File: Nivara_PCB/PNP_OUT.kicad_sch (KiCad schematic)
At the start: 0 parts

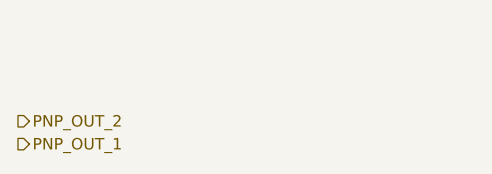
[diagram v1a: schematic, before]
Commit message: Añadido de funciones NPN/PNP
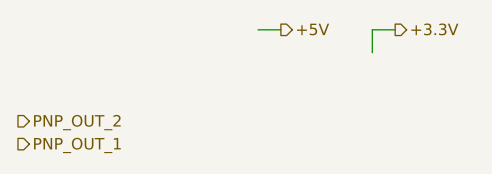
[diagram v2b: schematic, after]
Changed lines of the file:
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@@
 	(generator_version "9.0")
 	(paper "A4")
+	(wire
+		(pts
+			(xy 83.82 44.45) (xy 86.36 44.45)
+		)
+		(stroke
+			(width 0)
+			(type default)
+		)
+	)
+	(wire
+		(pts
+			(xy 96.52 44.45) (xy 96.52 46.99)
+		)
+		(stroke
+			(width 0)
+			(type default)
+		)
+	)
+	(wire
+		(pts
+			(xy 99.06 44.45) (xy 96.52 44.45)
+		)
+		(stroke
+			(width 0)
+			(type default)
+		)
+	)
+	(hierarchical_label "+5V"
+		(shape output)
+		(at 86.36 44.45 0)
+		(effects
+			(font
+				(size 1.27 1.27)
+			)
+			(justify left)
+		)
+	)
+	(hierarchical_label "+3.3V"
+		(shape output)
+		(at 99.06 44.45 0)
+		(effects
+			(font
+				(size 1.27 1.27)
+			)
+			(justify left)
+		)
+	)
 	(hierarchical_label "PNP_OUT_2"
 		(shape output)

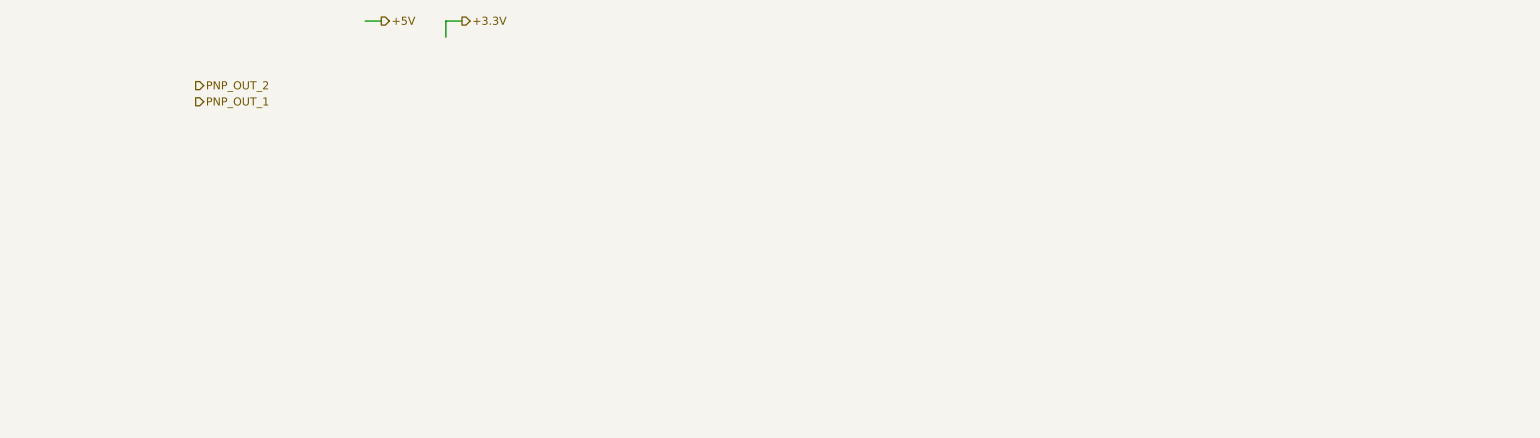
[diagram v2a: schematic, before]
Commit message: Cambios en el esquema de NPN y PNP
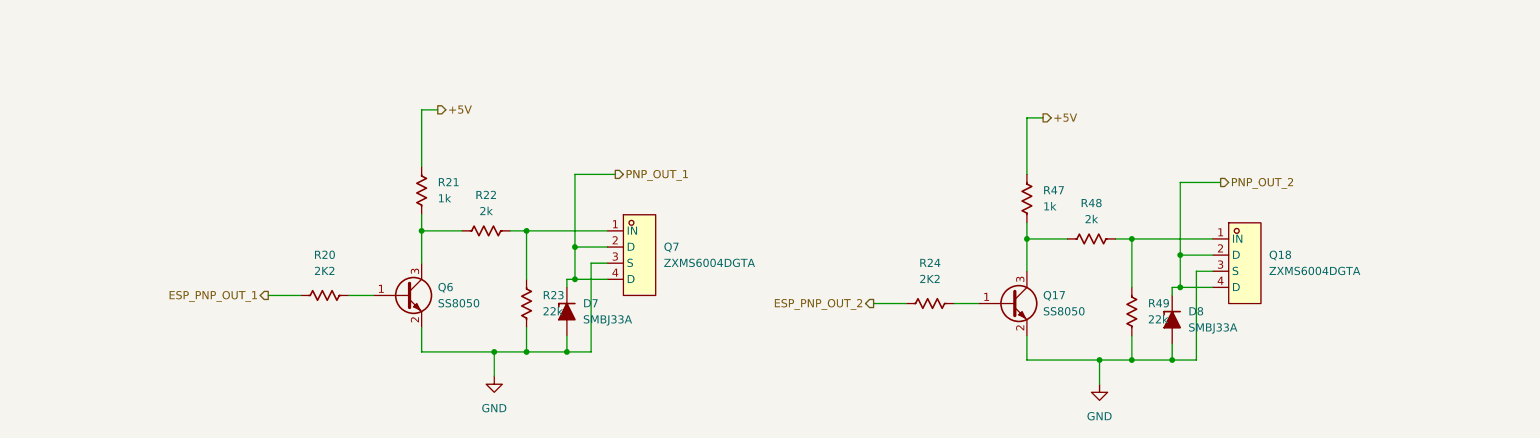
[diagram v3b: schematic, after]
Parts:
- added D7, D8: SMBJ33A, PCM_Diode_SMD_AKL:D_SMB, symbol PCM_Diode_TVS_AKL:SMBJ33A
- added Q17, Q6: SS8050, Package_TO_SOT_SMD:SOT-23, symbol Transistor_BJT:SS8050
- added Q18, Q7: ZXMS6004DGTA, Fuse_Holder:SOT-223-3_L6.5-W3.4-P2.30-LS7.0-BR, symbol Fuse_Holder:ZXMS6004DGTA
- added R20, R24: 2K2, PCM_Resistor_SMD_AKL:R_0603_1608Metric, symbol PCM_Resistor_US_AKL:R_0603
- added R21, R47: 1k, PCM_Resistor_SMD_AKL:R_0603_1608Metric, symbol PCM_Resistor_US_AKL:R_0603
- added R22, R48: 2k, PCM_Resistor_SMD_AKL:R_0603_1608Metric, symbol PCM_Resistor_US_AKL:R_0603
- added R23, R49: 22k, PCM_Resistor_SMD_AKL:R_0603_1608Metric, symbol PCM_Resistor_US_AKL:R_0603
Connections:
- net +5V: now also R21.1, R47.1
- net PNP_OUT_1: now also D7.1 (K), Q7.2 (D), Q7.4 (D)
- net PNP_OUT_2: now also D8.1 (K), Q18.2 (D), Q18.4 (D)
- new net: Q18.1 (IN), R48.2, R49.2
- new net: Q7.1 (IN), R22.2, R23.2
- new net: Q6.3 (C), R21.2, R22.1
- new net: Q17.1 (B), R24.2
- new net: Q17.3 (C), R47.2, R48.1
- new net: Q6.1 (B), R20.2
- new net ESP_PNP_OUT_1: R20.1
- new net ESP_PNP_OUT_2: R24.1
- new net GND: D7.2 (A), D8.2 (A), Q17.2 (E), Q18.3 (S), Q6.2 (E), Q7.3 (S), R23.1, R49.1

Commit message: Cambio de IntelliFet, porque los que tenían no estaban disponibles.
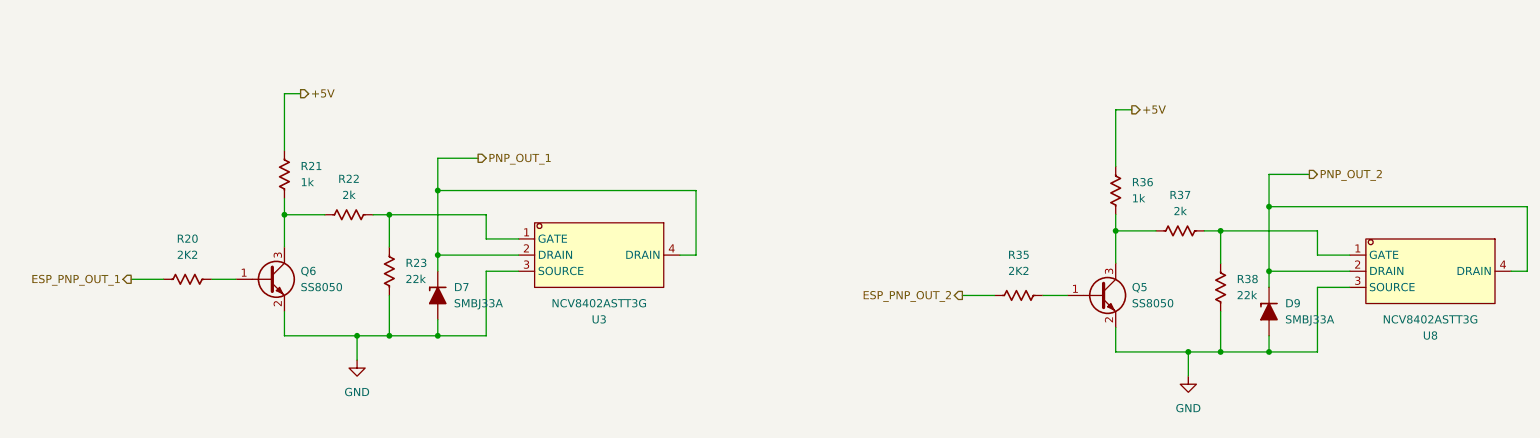
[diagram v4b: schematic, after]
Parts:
- removed D8: SMBJ33A, PCM_Diode_SMD_AKL:D_SMB, symbol PCM_Diode_TVS_AKL:SMBJ33A
- removed Q17: SS8050, Package_TO_SOT_SMD:SOT-23, symbol Transistor_BJT:SS8050
- removed Q18, Q7: ZXMS6004DGTA, Fuse_Holder:SOT-223-3_L6.5-W3.4-P2.30-LS7.0-BR, symbol Fuse_Holder:ZXMS6004DGTA
- removed R24: 2K2, PCM_Resistor_SMD_AKL:R_0603_1608Metric, symbol PCM_Resistor_US_AKL:R_0603
- removed R47: 1k, PCM_Resistor_SMD_AKL:R_0603_1608Metric, symbol PCM_Resistor_US_AKL:R_0603
- removed R48: 2k, PCM_Resistor_SMD_AKL:R_0603_1608Metric, symbol PCM_Resistor_US_AKL:R_0603
- removed R49: 22k, PCM_Resistor_SMD_AKL:R_0603_1608Metric, symbol PCM_Resistor_US_AKL:R_0603
- added D9: SMBJ33A, PCM_Diode_SMD_AKL:D_SMB, symbol PCM_Diode_TVS_AKL:SMBJ33A
- added Q5: SS8050, Package_TO_SOT_SMD:SOT-23, symbol Transistor_BJT:SS8050
- added R35: 2K2, PCM_Resistor_SMD_AKL:R_0603_1608Metric, symbol PCM_Resistor_US_AKL:R_0603
- added R36: 1k, PCM_Resistor_SMD_AKL:R_0603_1608Metric, symbol PCM_Resistor_US_AKL:R_0603
- added R37: 2k, PCM_Resistor_SMD_AKL:R_0603_1608Metric, symbol PCM_Resistor_US_AKL:R_0603
- added R38: 22k, PCM_Resistor_SMD_AKL:R_0603_1608Metric, symbol PCM_Resistor_US_AKL:R_0603
- added U3, U8: NCV8402ASTT3G, Fuse_Holder:SOT-223_L6.5-W3.5-P2.30-LS7.0-BR, symbol Fuse_Holder:NCV8402ASTT3G
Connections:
- net +5V: now also R36.1
- net ESP_PNP_OUT_2: now also R35.1
- net GND: now also D9.2 (A), Q5.2 (E), R38.1, U3.3 (SOURCE), U8.3 (SOURCE)
- net PNP_OUT_1: now also U3.2 (DRAIN), U3.4 (DRAIN)
- net PNP_OUT_2: now also D9.1 (K), U8.2 (DRAIN), U8.4 (DRAIN)
- net at R22.2, R23.2: now also U3.1 (GATE)
- new net: R37.2, R38.2, U8.1 (GATE)
- new net: Q5.3 (C), R36.2, R37.1
- new net: Q5.1 (B), R35.2
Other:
- moved on the sheet: D7, Q6, R20, R21, R22, R23

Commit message: Cambios en las salidas analogicas, ya que el ESP32 S3 no tiene DAC
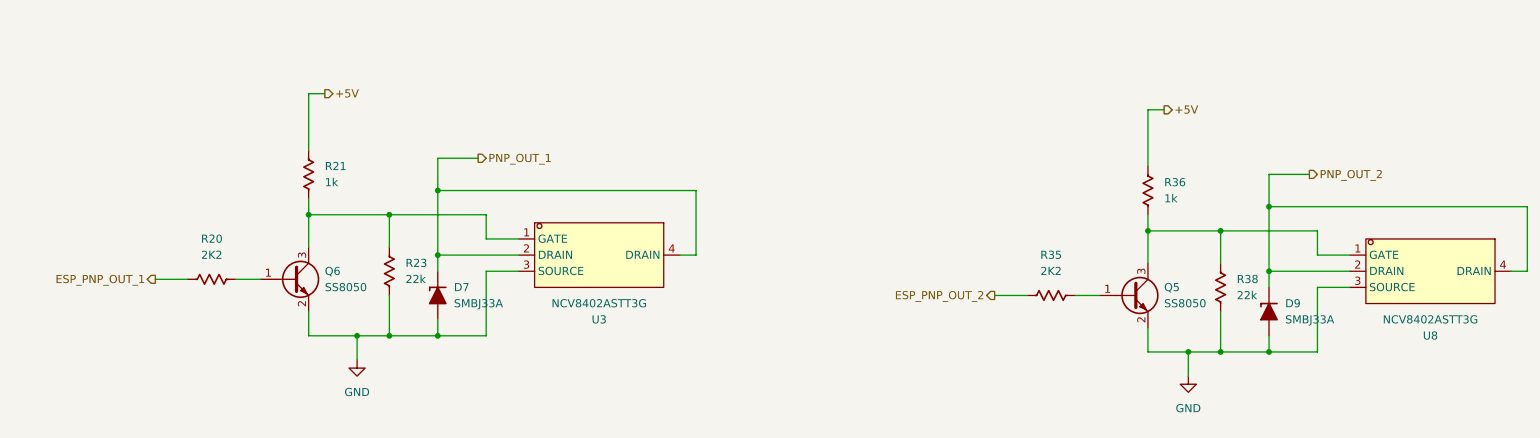
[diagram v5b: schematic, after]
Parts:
- removed R22, R37: 2k, PCM_Resistor_SMD_AKL:R_0603_1608Metric, symbol PCM_Resistor_US_AKL:R_0603
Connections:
- net at R38.2, U8.1 (GATE): now also Q5.3 (C), R36.2
- net at R23.2, U3.1 (GATE): now also Q6.3 (C), R21.2
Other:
- moved on the sheet: Q5, Q6, R20, R21, R35, R36

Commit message: Cambios en la medición de voltaje y corriente de la PCB Nivara.
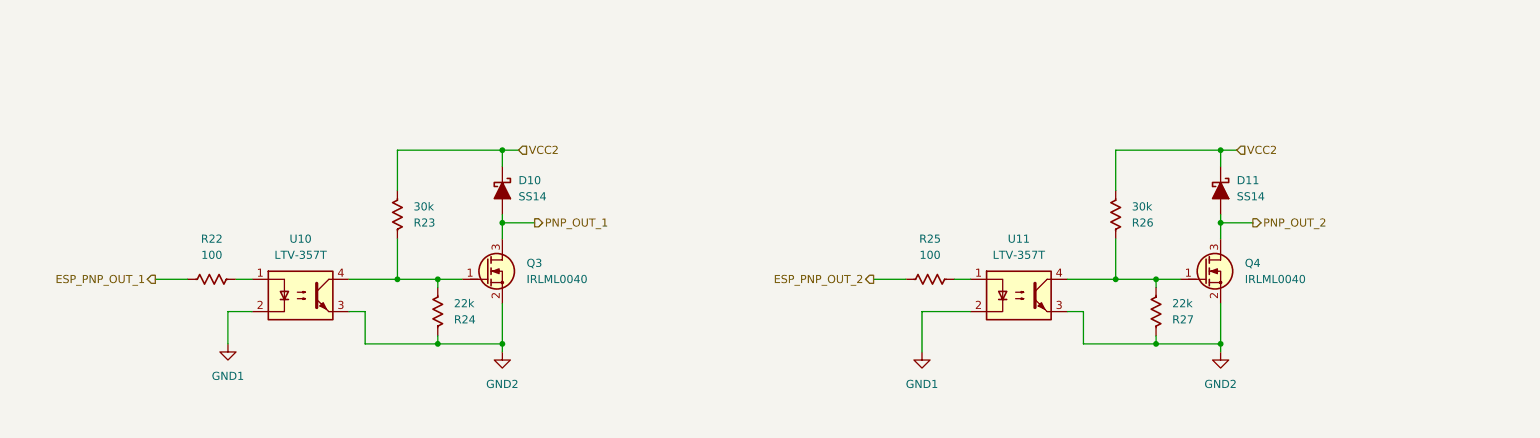
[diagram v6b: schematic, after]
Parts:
- removed D7, D9: SMBJ33A, PCM_Diode_SMD_AKL:D_SMB, symbol PCM_Diode_TVS_AKL:SMBJ33A
- removed Q5, Q6: SS8050, Package_TO_SOT_SMD:SOT-23, symbol Transistor_BJT:SS8050
- removed R20, R35: 2K2, PCM_Resistor_SMD_AKL:R_0603_1608Metric, symbol PCM_Resistor_US_AKL:R_0603
- removed R21, R36: 1k, PCM_Resistor_SMD_AKL:R_0603_1608Metric, symbol PCM_Resistor_US_AKL:R_0603
- removed R38: 22k, PCM_Resistor_SMD_AKL:R_0603_1608Metric, symbol PCM_Resistor_US_AKL:R_0603
- removed U3, U8: NCV8402ASTT3G, Fuse_Holder:SOT-223_L6.5-W3.5-P2.30-LS7.0-BR, symbol Fuse_Holder:NCV8402ASTT3G
- added D10, D11: SS14, PCM_Diode_SMD_AKL:D_SMA, symbol PCM_Diode_Schottky_AKL:SS14
- added Q3, Q4: IRLML0040, PCM_Package_TO_SOT_SMD_AKL:SOT-23, symbol PCM_Transistor_MOSFET_AKL:IRLML0040
- added R22, R25: 100, PCM_Resistor_SMD_AKL:R_0603_1608Metric, symbol PCM_Resistor_US_AKL:R_0603
- added R24, R27: 22k, PCM_Resistor_SMD_AKL:R_0603_1608Metric, symbol PCM_Resistor_US_AKL:R_0603
- added R26: 30k, PCM_Resistor_SMD_AKL:R_0603_1608Metric, symbol PCM_Resistor_US_AKL:R_0603
- added U10, U11: LTV-357T, Package_SO:SO-4_4.4x3.6mm_P2.54mm, symbol Isolator:LTV-357T
- R23: value 22k -> 30k
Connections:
- net ESP_PNP_OUT_1: now also R22.1
- net ESP_PNP_OUT_2: now also R25.1
- net PNP_OUT_1: now also D10.2 (A), Q3.3 (D)
- net PNP_OUT_2: now also D11.2 (A), Q4.3 (D)
- net VCC2: now reaches R23.2
- net VCC2: now also D10.1 (K), D11.1 (K), R26.2
- net GND: no longer names the net of R23.1
- net GND: now also Q3.1 (G), R24.2, U10.4
- new net: Q4.1 (G), R26.1, R27.2, U11.4
- new net: R22.2, U10.1
- new net: R25.2, U11.1
- new net GND1: U10.2, U11.2
- new net GND2: Q3.2 (S), Q4.2 (S), R24.1, R27.1, U10.3, U11.3

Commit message: New changes to the Nivara PCB schematic files.
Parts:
- added D29, D30: LED ON, LED_SMD:LED_0603_1608Metric, symbol Device:LED
- added R56, R57: 1.5k, PCM_Resistor_SMD_AKL:R_0603_1608Metric, symbol PCM_Resistor_US_AKL:R_0603
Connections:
- net PNP_OUT_1: now also D29.1 (K)
- net PNP_OUT_2: now also D30.1 (K)
- net VCC2: now also R56.1, R57.1
- new net: D29.2 (A), R56.2
- new net: D30.2 (A), R57.2
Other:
- moved on the sheet: D10

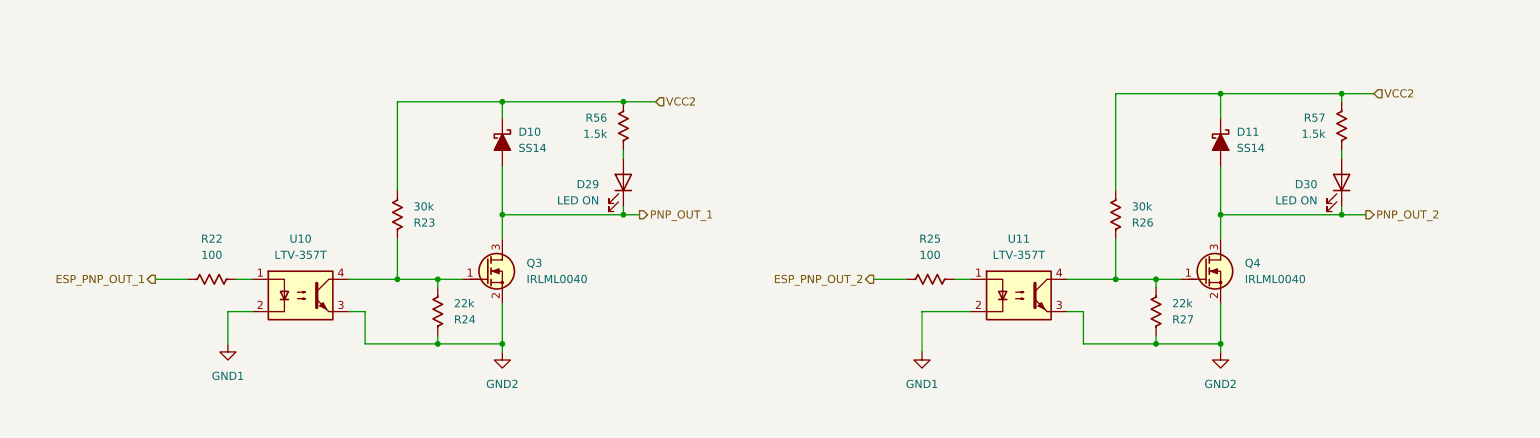
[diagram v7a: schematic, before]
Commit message: Cambios en el PCB de Nivara. Ruteo de emtradas y salidas NPN y PNP.
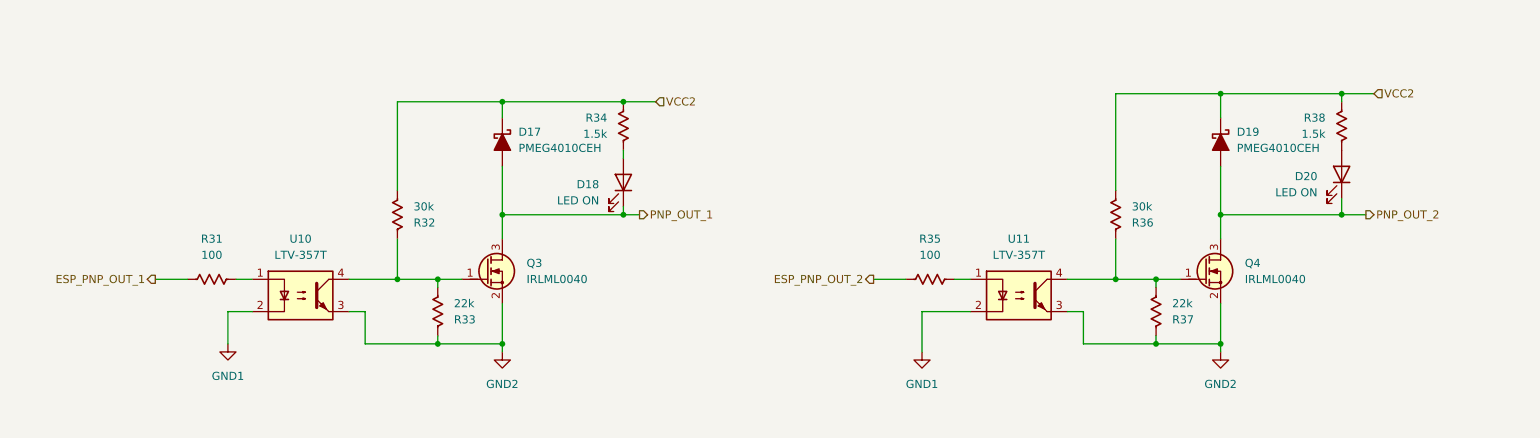
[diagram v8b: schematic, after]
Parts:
- removed D10, D11: SS14, PCM_Diode_SMD_AKL:D_SMA, symbol PCM_Diode_Schottky_AKL:SS14
- added D17, D19: PMEG4010CEH, PCM_Diode_SMD_AKL:D_SOD-123F, symbol PCM_Diode_Schottky_AKL:PMEG4010CEH
- renumbered D29 to D18, D30 to D20, R22 to R31, R23 to R32, R24 to R33, R56 to R34, R25 to R35, R26 to R36, R27 to R37, R57 to R38
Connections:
- net PNP_OUT_1: now also D17.2 (A)
- net PNP_OUT_2: now also D19.2 (A)
- net VCC2: now also D17.1 (K), D19.1 (K)
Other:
- moved on the sheet: D20
